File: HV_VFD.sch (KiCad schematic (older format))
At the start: 3 parts, among them Q1 SEMiX402GB066HDs, Q2 SEMiX402GB066HDs, Q3 SEMiX402GB066HDs

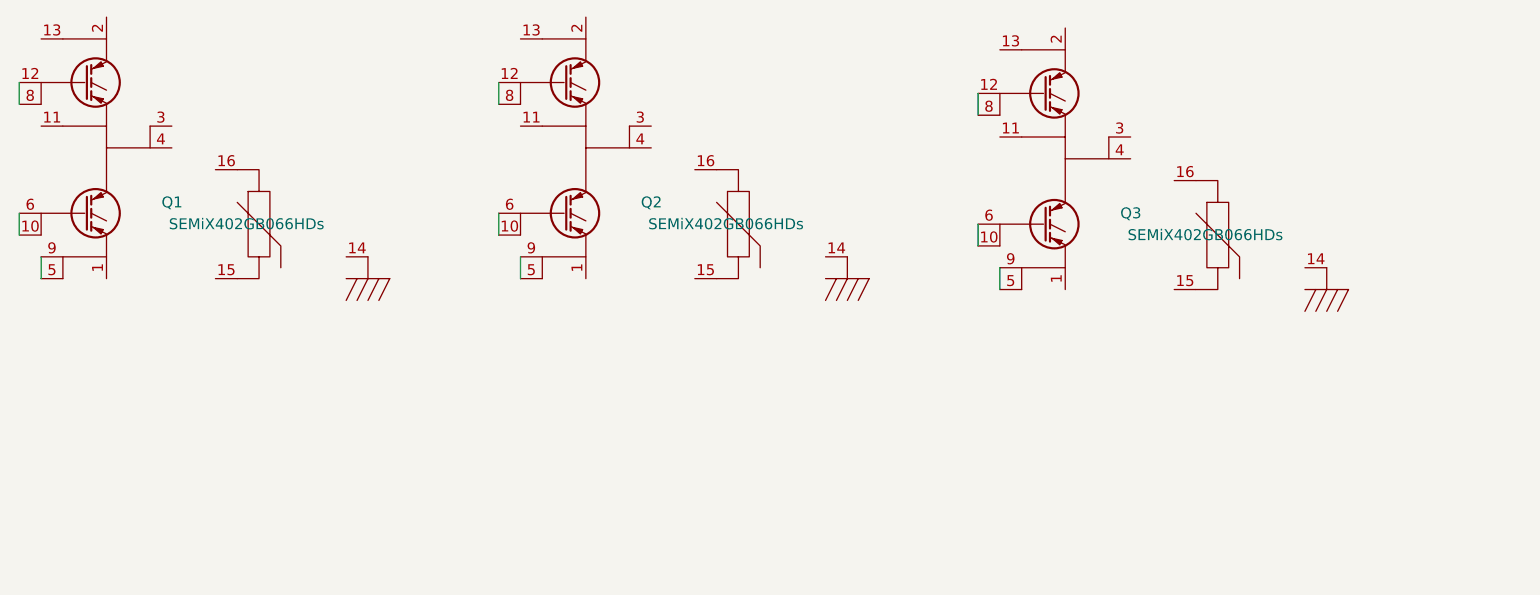
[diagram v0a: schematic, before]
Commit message: added basic bootstrap and desat diodes
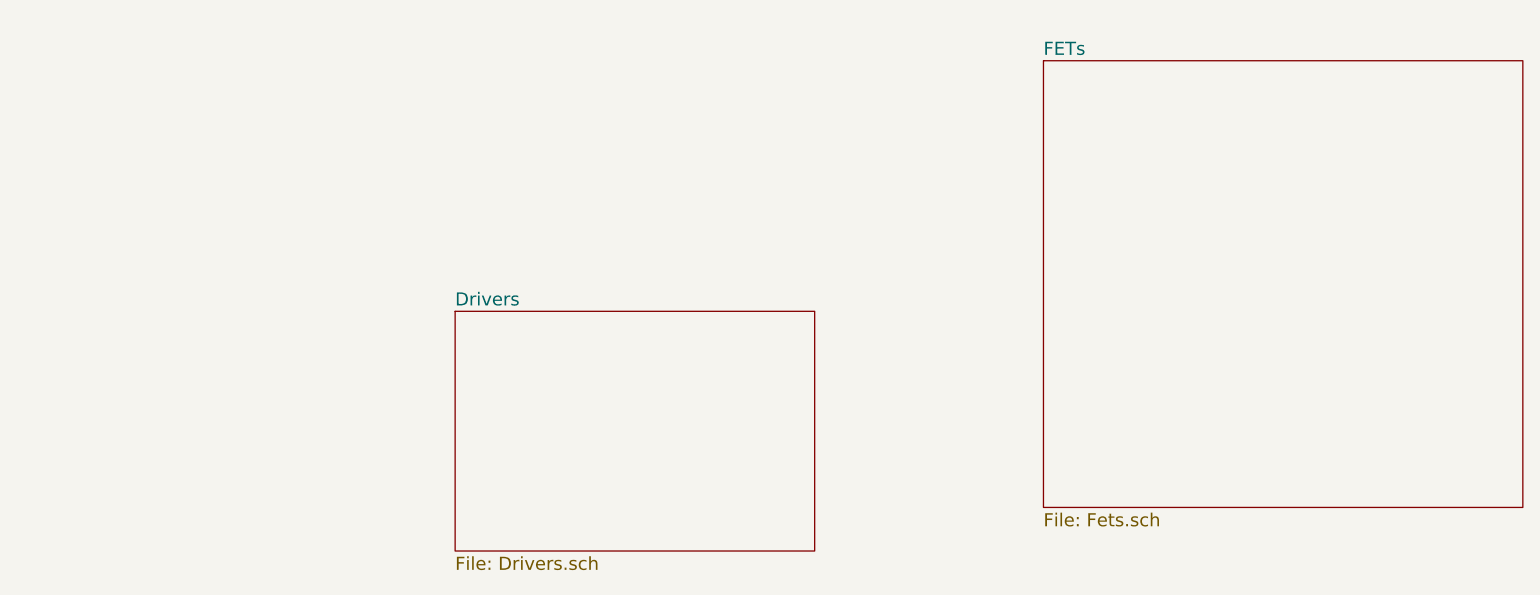
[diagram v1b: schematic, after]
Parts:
- removed Q1, Q2, Q3: SEMiX402GB066HDs, VFD_parts:SEMiX_2s, symbol SEMiX402GB066HDs
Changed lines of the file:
@@
 $Descr A4 11693 8268
 encoding utf-8
-Sheet 1 1
+Sheet 1 3
 Title ""
 Date ""
@@
 Comment4 ""
 $EndDescr
-$Comp
-L SEMiX402GB066HDs Q1
-U 1 1 5768DC11
-P 4200 2350
-F 0 "Q1" H 4650 1800 50  0000 R CNN
-F 1 "SEMiX402GB066HDs" H 5300 1700 50  0000 R CNN
-F 2 "VFD_parts:SEMiX_2s" H 4400 2450 50  0001 C CNN
-F 3 "" H 4200 2350 50  0000 C CNN
-	1    4200 2350
-	1    0    0    -1
-$EndComp
-$Comp
-L SEMiX402GB066HDs Q2
-U 1 1 5768DCA2
-P 6400 2350
-F 0 "Q2" H 6850 1800 50  0000 R CNN
-F 1 "SEMiX402GB066HDs" H 7500 1700 50  0000 R CNN
-F 2 "VFD_parts:SEMiX_2s" H 6600 2450 50  0001 C CNN
-F 3 "" H 6400 2350 50  0000 C CNN
-	1    6400 2350
-	1    0    0    -1
-$EndComp
-$Comp
-L SEMiX402GB066HDs Q3
-U 1 1 5768DCDC
-P 8600 2400
-F 0 "Q3" H 9050 1850 50  0000 R CNN
-F 1 "SEMiX402GB066HDs" H 9700 1750 50  0000 R CNN
-F 2 "VFD_parts:SEMiX_2s" H 8800 2500 50  0001 C CNN
-F 3 "" H 8600 2400 50  0000 C CNN
-	1    8600 2400
-	1    0    0    -1
-$EndComp
-Wire Wire Line
-	6100 2350 6100 2450
-Wire Wire Line
-	6100 2950 6100 3050
-Wire Wire Line
-	6200 3150 6200 3250
-Wire Wire Line
-	8300 2400 8300 2500
-Wire Wire Line
-	8300 3000 8300 3100
-Wire Wire Line
-	8400 3200 8400 3300
-Wire Wire Line
-	3900 2350 3900 2450
-Wire Wire Line
-	3900 2950 3900 3050
-Wire Wire Line
-	4000 3150 4000 3250
+$Sheet
+S 8600 2250 2200 2050
+U 576A744A
+F0 "FETs" 60
+F1 "Fets.sch" 60
+$EndSheet
+$Sheet
+S 5900 3400 1650 1100
+U 576A7A92
+F0 "Drivers" 60
+F1 "Drivers.sch" 60
+$EndSheet
 $EndSCHEMATC
